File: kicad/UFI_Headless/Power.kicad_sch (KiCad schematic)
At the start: 35 parts, among them J1 USB-C, J2 12V DC 5.5/2.1, J3 FDD_PWR, U1 USBLC6-2SC6, U2 TPS54202DDC, U3 TPS2116DRL, U4 AP7361C-33E

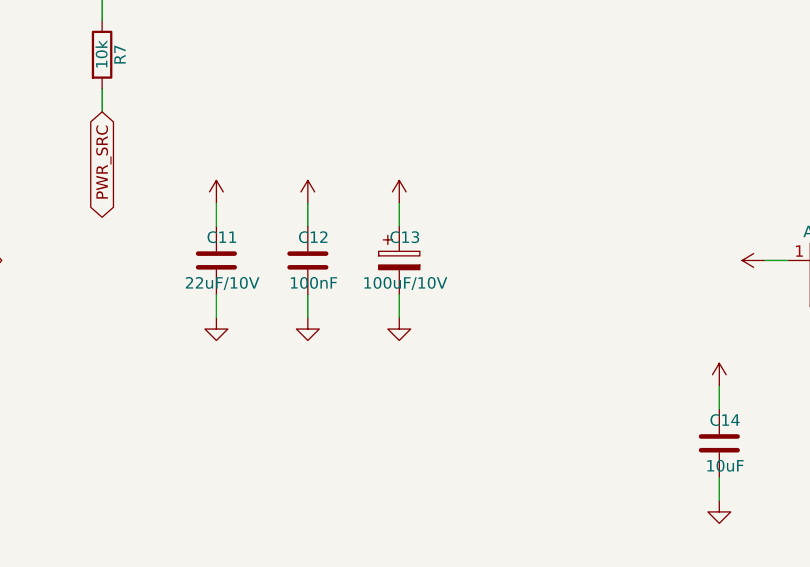
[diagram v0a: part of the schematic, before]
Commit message: UFI Headless: 4-layer layout v0.1, LCSC sourcing, fab outputs
- build_pcb.py: footprints from the schematic netlist (KIID-linked), placement,
  pre-routed USB-C fan-out and MCU VSS stubs, In1 GND plane
- make_pcb.sh: Freerouting 2.4.1 routing, violation cleanup, supply widening,
  GND/3V3 pours, stitching vias; DRC 0 errors, schematic parity clean
- LCSC part numbers via JLCPCB API; crystal X322525MOB4SI (CL 12pF, 2x 18pF)
- fertigung/: Gerber, Excellon, BOM/CPL (KiCad + JLC format)

Co-Authored-By: Claude Opus 5.5 <noreply@anthropic.com>
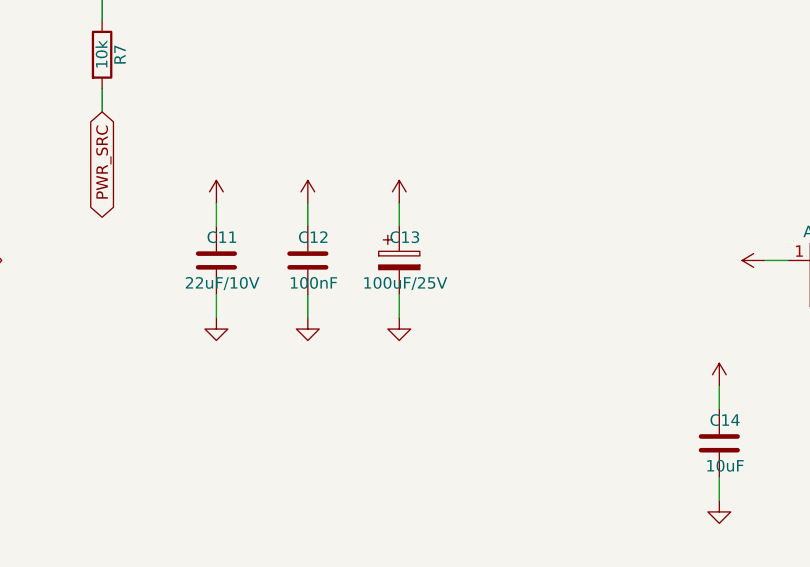
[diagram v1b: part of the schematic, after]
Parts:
- C1: LCSC (none) -> C5337554
- C10, C8, C9: LCSC (none) -> C15849
- C11: LCSC (none) -> C45783
- C12, C16, C3, C4, C7: LCSC (none) -> C14663
- C13: value 100uF/10V -> 100uF/25V; LCSC (none) -> C5337554
- C14, C15: LCSC (none) -> C15850
- C2: LCSC (none) -> C454102
- C5, C6: LCSC (none) -> C90146
- D1: LCSC (none) -> C2980402
- D2: LCSC (none) -> C16103; MPN SS54 (40V/5A) -> SS54C (40V/5A)
- D3: LCSC (none) -> C110044
- F1: LCSC (none) -> C32404; MPN Polyfuse 1812 1.5A/6V -> SMD1812P150TF/24 (1.5A hold)
- J1: footprint Connector_USB:USB_C_Receptacle_GCT_USB4105-xx-A_16P_TopMnt_Horizontal -> Connector_USB:USB_C_Receptacle_HRO_TYPE-C-31-M-12; LCSC (none) -> C165948; MPN GCT USB4105-GF-A -> HRO TYPE-C-31-M-12
- J3: LCSC (none) -> C32713270
- L1: LCSC (none) -> C1330797
- R1, R2: LCSC (none) -> C23186
- R3: LCSC (none) -> C25803
- R4: LCSC (none) -> C25952
- R5: LCSC (none) -> C4216
- R6, R7: LCSC (none) -> C25804
- U1: LCSC (none) -> C7519
- U2: LCSC (none) -> C191884
- U3: LCSC (none) -> C3235557
- U4: LCSC (none) -> C500795

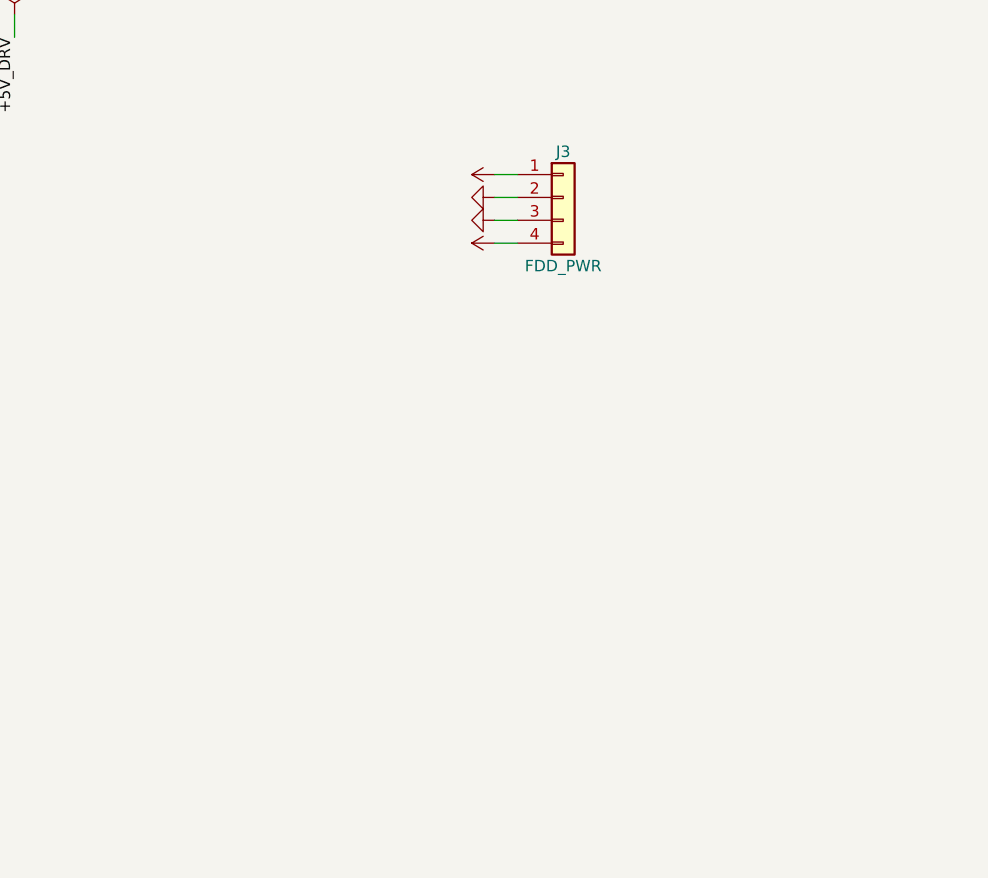
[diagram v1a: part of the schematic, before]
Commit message: UFI Headless v0.2: 8 MB PSRAM, ESD, drive polyfuses, test points
Schematic (new parts get fixed references above the v0.1 maxima, so all
existing references and PCB links stay unchanged):
- U11 APS6404L 8 MB QSPI PSRAM on OCTOSPIM P1 (PB2/PB10/PD11/PD12/PB13/
  PD13), C46, CE# pull-up R16
- D9-D11 ESDA6V1-5SC6 on the 13 Amiga J7 bus lines + MOTOR_A, D12 on IEC
- F2/F3 polyfuses: drive supplies FDD_5V/FDD_12V for J3 and J7 pins 12/23
- TP1-TP6 (3V3, 5V, 12V, GND, RDATA, INDEX), excluded from BOM/CPL
Layout (incremental ECO on the reviewed board):
- scripts/add_parts.py: re-net pads, collision-aware placement, rip up only
  what is in the way; make_pcb.sh 'eco' step
- fixes found on the way: supply pours ran after finish_pcb and left GND
  islands (LDO U4 ground!) without vias -> order swapped, GND pour check
  per net; island/dogbone vias never inside pads; manual_routes no longer
  re-applies the D+ fallback; pipeline filters robust against interleaved
  SWIG noise under pipefail
- DRC rule for the intentional J6/J7 silk overhang instead of warnings;
  netclasses cover the new drive supply nets
DRC: 0 errors, 0 warnings, 0 unconnected, parity clean, no via-in-pad.

Co-Authored-By: Claude Opus 5.5 <noreply@anthropic.com>
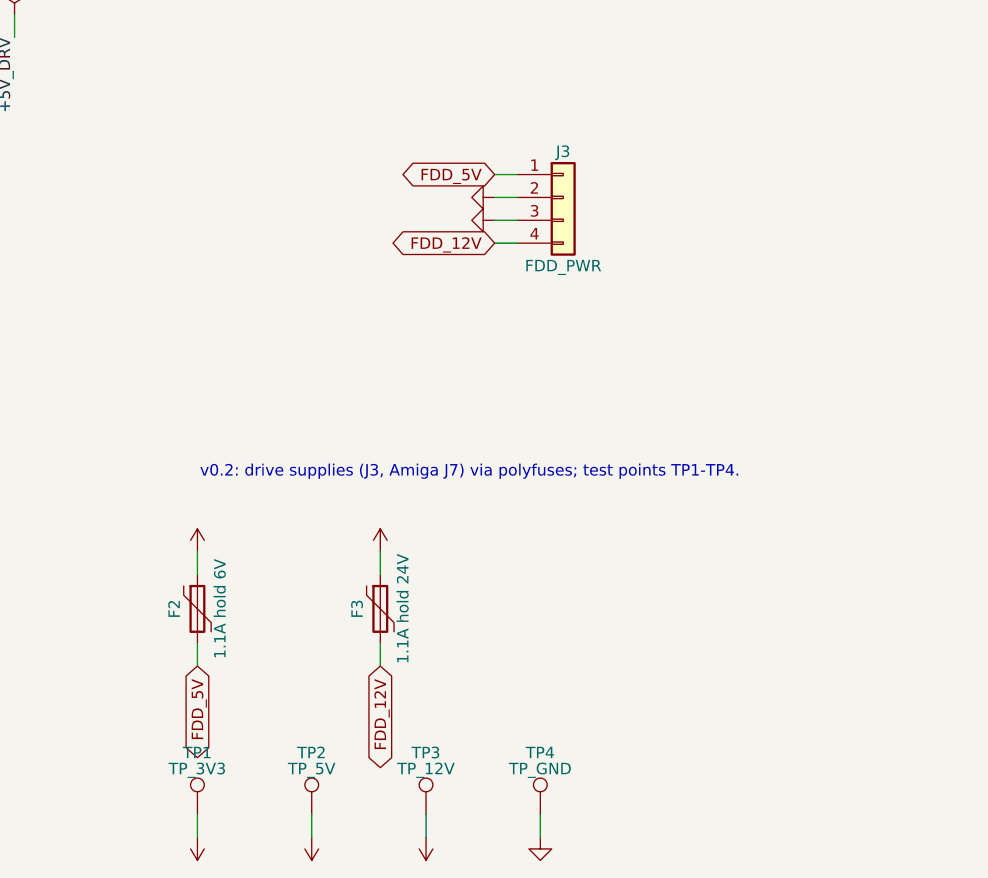
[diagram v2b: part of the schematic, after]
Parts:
- added F2: 1.1A hold 6V, Fuse:Fuse_1206_3216Metric, symbol Device:Polyfuse
- added F3: 1.1A hold 24V, Fuse:Fuse_1812_4532Metric, symbol Device:Polyfuse
- added TP1: TP_3V3, TestPoint:TestPoint_Pad_D1.5mm, symbol Connector:TestPoint
- added TP2: TP_5V, TestPoint:TestPoint_Pad_D1.5mm, symbol Connector:TestPoint
- added TP3: TP_12V, TestPoint:TestPoint_Pad_D1.5mm, symbol Connector:TestPoint
- added TP4: TP_GND, TestPoint:TestPoint_Pad_D1.5mm, symbol Connector:TestPoint
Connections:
- net +12V: now also F3.1, TP3.1; no longer J3.4 (Pin_4)
- net +3V3: now also TP1.1
- net +5V: now also F2.1, TP2.1; no longer J3.1 (Pin_1)
- net GND: now also TP4.1
- new net FDD_12V: F3.2, J3.4 (Pin_4)
- new net FDD_5V: F2.2, J3.1 (Pin_1)
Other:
- note added: "v0.2: drive supplies (J3, Amiga J7) via polyfuses; test points TP1-TP4."

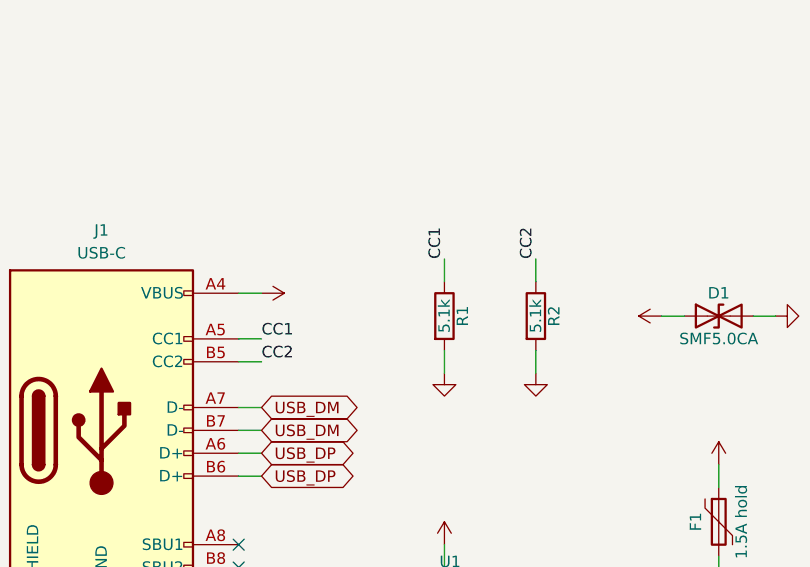
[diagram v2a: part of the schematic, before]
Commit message: UFI Headless v0.3: USB-C source current detection
- schematic: CC1/CC2 (Rd 5.1k) also to PA0/PA3 (ADC1 INP16/INP15); ECO
  routed on the reviewed board, DRC 0 errors / 0 warnings, parity clean
- firmware: USB_POWER (0x19) measures CC voltages, reports the allowed
  source current (0.5 / 1.5 / 3 A per Type-C vRd ranges)
- host tool: ufi usb-power
- manual_routes: D+ fallback skipped when any D+ via is near its start
  (Freerouting's own via sits 0.25 mm away; it was re-added every run)
- README: CC pins, Atari SIO option on existing UART pins (PD1/PF6/PD0)

Co-Authored-By: Claude Opus 5.5 <noreply@anthropic.com>
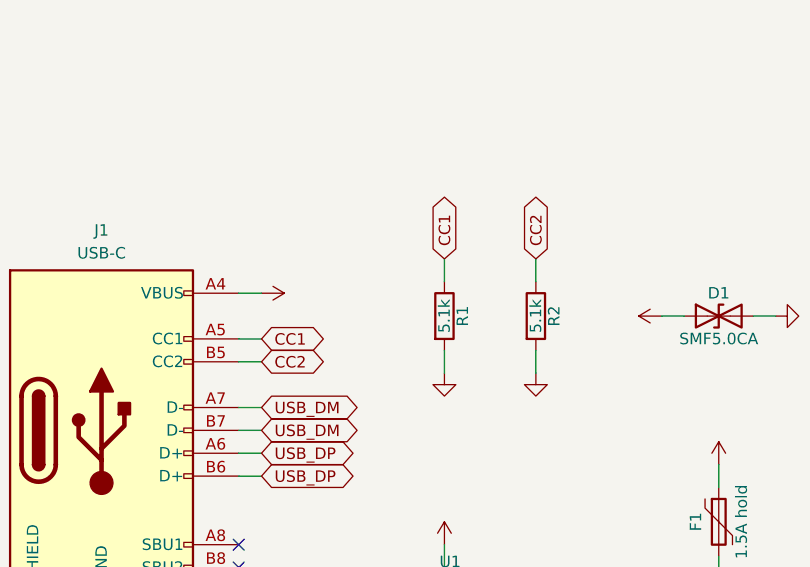
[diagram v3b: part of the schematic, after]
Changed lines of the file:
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@@
 (wire (pts (xy 55.88 73.66) (xy 58.42 73.66)) (stroke (width 0) (type default)))
 (wire (pts (xy 55.88 78.74) (xy 58.42 78.74)) (stroke (width 0) (type default)))
-(label "CC1" (at 58.42 78.74 0) (fields_autoplaced yes) (effects (font (size 1.27 1.27)) (justify left bottom)))
+(global_label "CC1" (shape bidirectional) (at 58.42 78.74 0) (fields_autoplaced yes) (effects (font (size 1.27 1.27)) (justify left)) (property "Intersheetrefs" "${INTERSHEET_REFS}" (at 58.42 78.74 0) (effects (font (size 1.27 1.27)) (hide yes))))
 (wire (pts (xy 55.88 91.44) (xy 58.42 91.44)) (stroke (width 0) (type default)))
 (global_label "USB_DP" (shape bidirectional) (at 58.42 91.44 0) (fields_autoplaced yes) (effects (font (size 1.27 1.27)) (justify left)) (property "Intersheetrefs" "${INTERSHEET_REFS}" (at 58.42 91.44 0) (effects (font (size 1.27 1.27)) (hide yes))))
@@
 (no_connect (at 55.88 101.6))
 (wire (pts (xy 55.88 81.28) (xy 58.42 81.28)) (stroke (width 0) (type default)))
-(label "CC2" (at 58.42 81.28 0) (fields_autoplaced yes) (effects (font (size 1.27 1.27)) (justify left bottom)))
+(global_label "CC2" (shape bidirectional) (at 58.42 81.28 0) (fields_autoplaced yes) (effects (font (size 1.27 1.27)) (justify left)) (property "Intersheetrefs" "${INTERSHEET_REFS}" (at 58.42 81.28 0) (effects (font (size 1.27 1.27)) (hide yes))))
 (wire (pts (xy 55.88 93.98) (xy 58.42 93.98)) (stroke (width 0) (type default)))
 (global_label "USB_DP" (shape bidirectional) (at 58.42 93.98 0) (fields_autoplaced yes) (effects (font (size 1.27 1.27)) (justify left)) (property "Intersheetrefs" "${INTERSHEET_REFS}" (at 58.42 93.98 0) (effects (font (size 1.27 1.27)) (hide yes))))
@@
 (wire (pts (xy 33.02 111.76) (xy 33.02 114.3)) (stroke (width 0) (type default)))
 (wire (pts (xy 78.74 72.39) (xy 78.74 69.85)) (stroke (width 0) (type default)))
-(label "CC1" (at 78.74 69.85 90) (fields_autoplaced yes) (effects (font (size 1.27 1.27)) (justify left bottom)))
+(global_label "CC1" (shape bidirectional) (at 78.74 69.85 90) (fields_autoplaced yes) (effects (font (size 1.27 1.27)) (justify left)) (property "Intersheetrefs" "${INTERSHEET_REFS}" (at 78.74 69.85 0) (effects (font (size 1.27 1.27)) (hide yes))))
 (wire (pts (xy 78.74 80.01) (xy 78.74 82.55)) (stroke (width 0) (type default)))
 (wire (pts (xy 88.9 72.39) (xy 88.9 69.85)) (stroke (width 0) (type default)))
-(label "CC2" (at 88.9 69.85 90) (fields_autoplaced yes) (effects (font (size 1.27 1.27)) (justify left bottom)))
+(global_label "CC2" (shape bidirectional) (at 88.9 69.85 90) (fields_autoplaced yes) (effects (font (size 1.27 1.27)) (justify left)) (property "Intersheetrefs" "${INTERSHEET_REFS}" (at 88.9 69.85 0) (effects (font (size 1.27 1.27)) (hide yes))))
 (wire (pts (xy 88.9 80.01) (xy 88.9 82.55)) (stroke (width 0) (type default)))
 (wire (pts (xy 73.66 109.22) (xy 71.12 109.22)) (stroke (width 0) (type default)))
